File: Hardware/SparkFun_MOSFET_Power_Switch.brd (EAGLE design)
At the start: 35.6 x 34.3 mm, 56 parts, among them J3 5.5x2.1mm Barrel, Q1 600mA/40V, Q2 100A/100V/6.8mΩ, U1 LMR14203

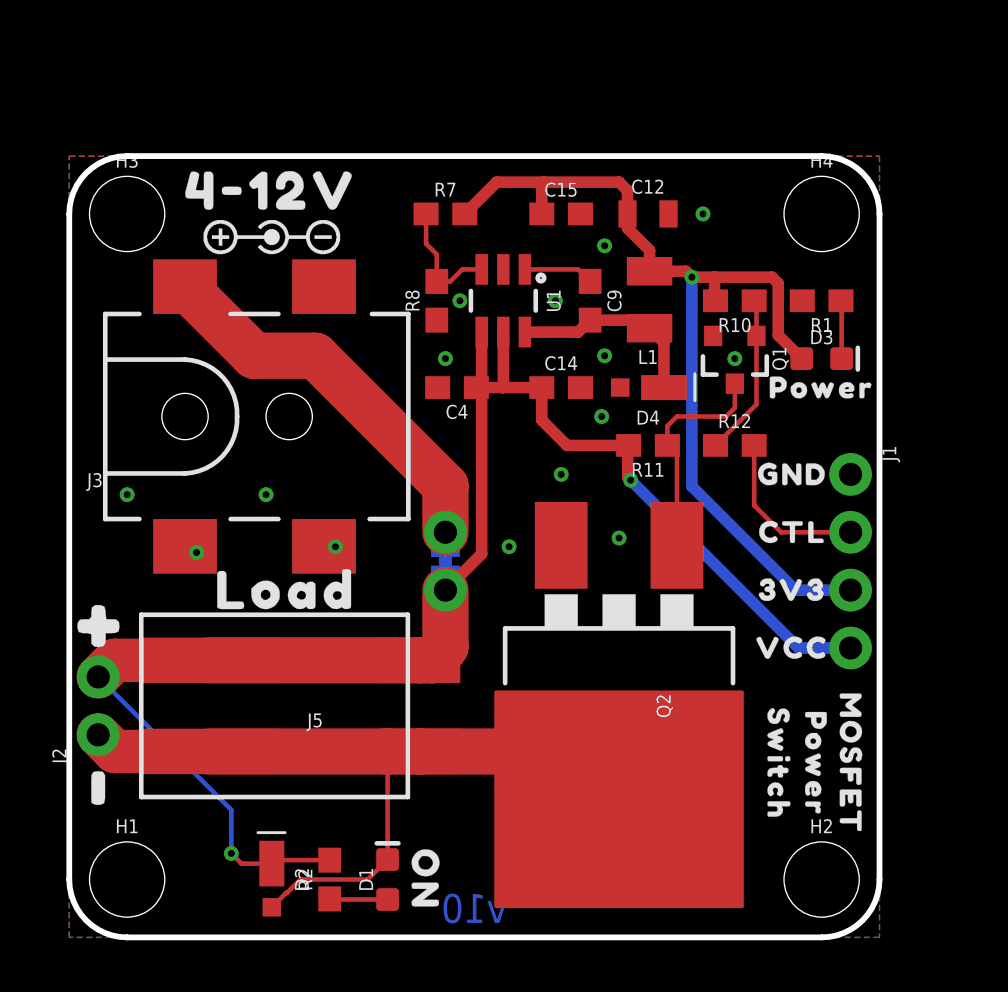
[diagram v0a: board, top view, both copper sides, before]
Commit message: add 4-pin female header
-added SMD vertical 4-pin header to allow solderless connection access to the CTRL line and more.
-Added jumpers to kill power and on LEDs
-updated silk to inverted buzzard style
-changed logo to SFE
-updated measures.
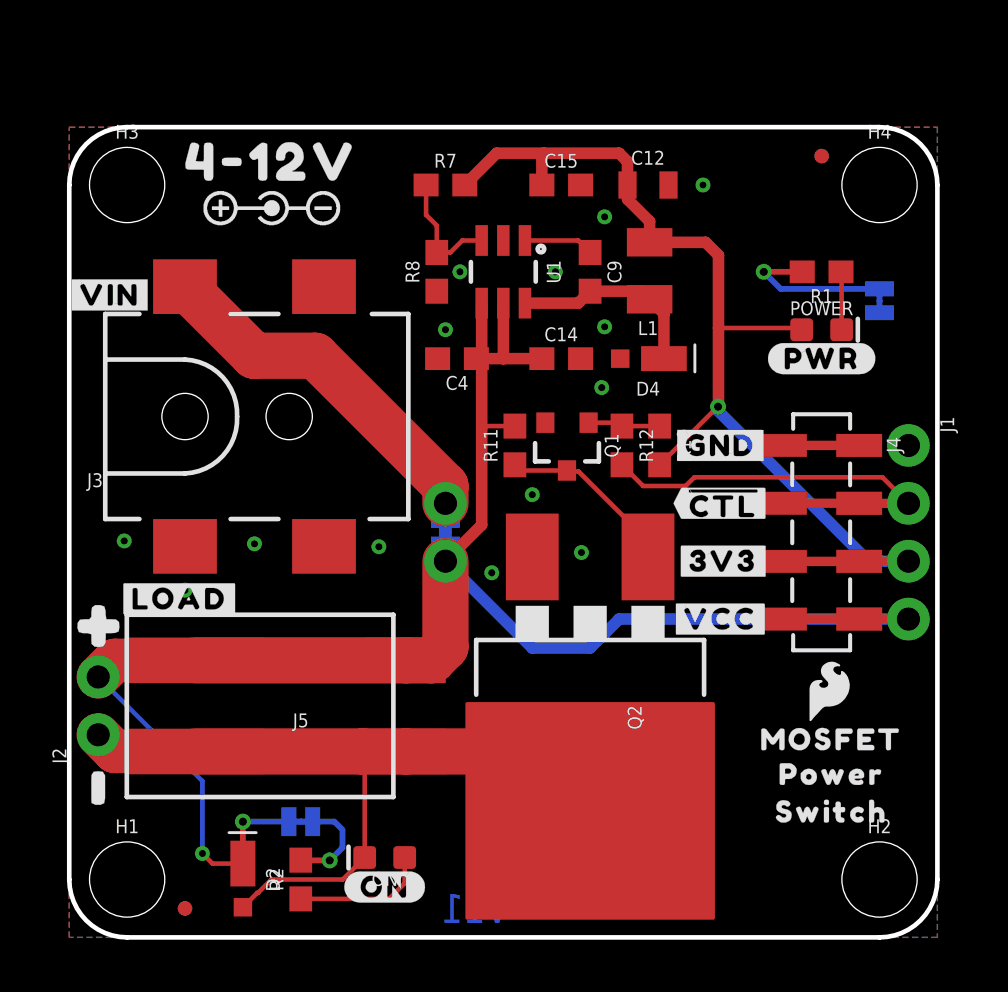
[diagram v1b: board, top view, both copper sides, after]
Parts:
- removed D1, D3: RED, SparkFun-LED:LED-0603
- removed JP2: JUMPER-COMBO_2_NC_TRACE, SparkFun-Jumpers:COMBO-JUMPER_2_NC_TRACE
- removed U$23: (no value), output:POWER0
- removed U$49: (no value), output:ON0
- added FD1, FD2, FD3, FD4: FIDUCIALUFIDUCIAL, SparkFun-Aesthetics:FIDUCIAL-MICRO
- added J4: SMD, SparkFun-Connectors:1X04_SMD_VERTICAL_COMBO
- added LOGO2: SFE_LOGO_NAME_FLAME.1_INCH, SparkFun-Aesthetics:SFE_LOGO_NAME_FLAME_.1
- added MEAS: JUMPER-COMBO_2_NC_TRACE, SparkFun-Jumpers:COMBO-JUMPER_2_NC_TRACE
- added ON, POWER: RED, SparkFun-LED:LED-0603
- added ON_LED, PWR_LED: (no value), SparkFun-Jumpers:SMT-JUMPER_2_NC_TRACE_SILK
- added U$12, U$4: (no value), output:#GND#0
- added U$14, U$27: (no value), output:#3V3#3
- added U$28: (no value), output:##CTL##1
- added U$30: (no value), output:##CTL##2
- added U$31, U$32: (no value), output:#VCC#4
- J1: value (none) -> PTH
- R7: value 3.3k -> 100k
- R8: value 1k -> 30.1k
- U$1: device output:3V32 -> output:#LOAD#7
- U$15: device output:GND0 -> output:#PWR_LED#11
- U$16: device output:CTL0 -> output:#ON_LED#13
- U$17: device output:3V32 -> output:#MEAS#14
- U$18: device output:VCC3 -> output:#VIN#8
- U$21: value SPARKX-LOGO5 -> (none); device SparkX:SPARKX-LARGE -> output:#VCC#4
- U$3: device output:GND0 -> output:#VIN#8
- U$5: device output:LOAD0 -> output:#PWR#9
- U$7: device output:VCC3 -> output:#ON#10
- U$8: device output:CTL0 -> SparkFun-Aesthetics:SFE_LOGO_FLAME_.1
- moved U$3 31.0 mm to (1.78, 28.2)
- moved U$1 26.9 mm to (4.83, 14.9)
- moved U$5 25.6 mm to (33.0, 25.4)
- moved U$16 21.0 mm to (14.8, 5.13)
- moved U$7 20.8 mm to (13.8, 2.21)
- moved U$18 18.6 mm to (14.1, 19.0)
- moved U$26 14.8 mm to (17.9, 22.5)
- moved U$25 14.6 mm to (18.0, 24.8)
- moved U$24 14.6 mm to (17.9, 27.3)
- moved U$17 13.7 mm to (18.2, 17.6), turned to 90 degrees
- moved U$21 13.3 mm to (13.9, 16.5)
- moved Q1 8.29 mm to (21.8, 21.6)
- moved U$15 7.67 mm to (30.6, 27.9)
- moved R10 7.16 mm to (25.9, 21.6), turned to 270 degrees
- moved U$8 7.14 mm to (33.4, 10.8)
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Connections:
- new net N$6: PWR_LED.2, R1.2
- new net N$7: ON_LED.1, R2.2
- net 3.3V: now also J4.3, POWER.A; no longer D3.A
- net CUTOFF: now also J4.2
- net GND: now also J4.1, PWR_LED.1; no longer R1.2
- net N$2: now also ON.A; no longer D1.A
- net N$3: now also POWER.C; no longer D3.C
- net SOLENOID: now also ON.C; no longer D1.C
- net VCC: now also J4.4, MEAS.2, MEAS.4, ON_LED.2; no longer JP2.2, JP2.4, R2.2
- net VIN: now also MEAS.1, MEAS.3; no longer JP2.1, JP2.3
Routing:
- net CUTOFF: track 7.35 -> 15.7 mm
- net VCC: track 71.0 -> 79.1 mm
- net N$6: track 0.00 -> 7.08 mm, vias 0 -> 1
- net N$7: track 0.00 -> 4.31 mm, vias 0 -> 1
- net N$12: track 7.14 -> 3.18 mm
- net N$2: track 2.55 -> 5.97 mm
- net 3.3V: track 41.9 -> 43.9 mm
- net N$1: track 9.76 -> 7.93 mm
- net VIN: track 18.0 -> 16.6 mm
- net SOLENOID: track 33.9 -> 33.1 mm
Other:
- board size 35.6 x 34.3 mm -> 38.1 x 35.6 mm
- board text added: "Nathan Seidle"
- board text added: "Revised by: Pete Lewis"
- board text added: "Units are INCHES"
- board text added: "v11"
- board text removed: "v10"

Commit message: Buck reg routing
-optimized buck reg routing
-added PTH header for VIN/GND
-added "low-side" to silk name top and bottom
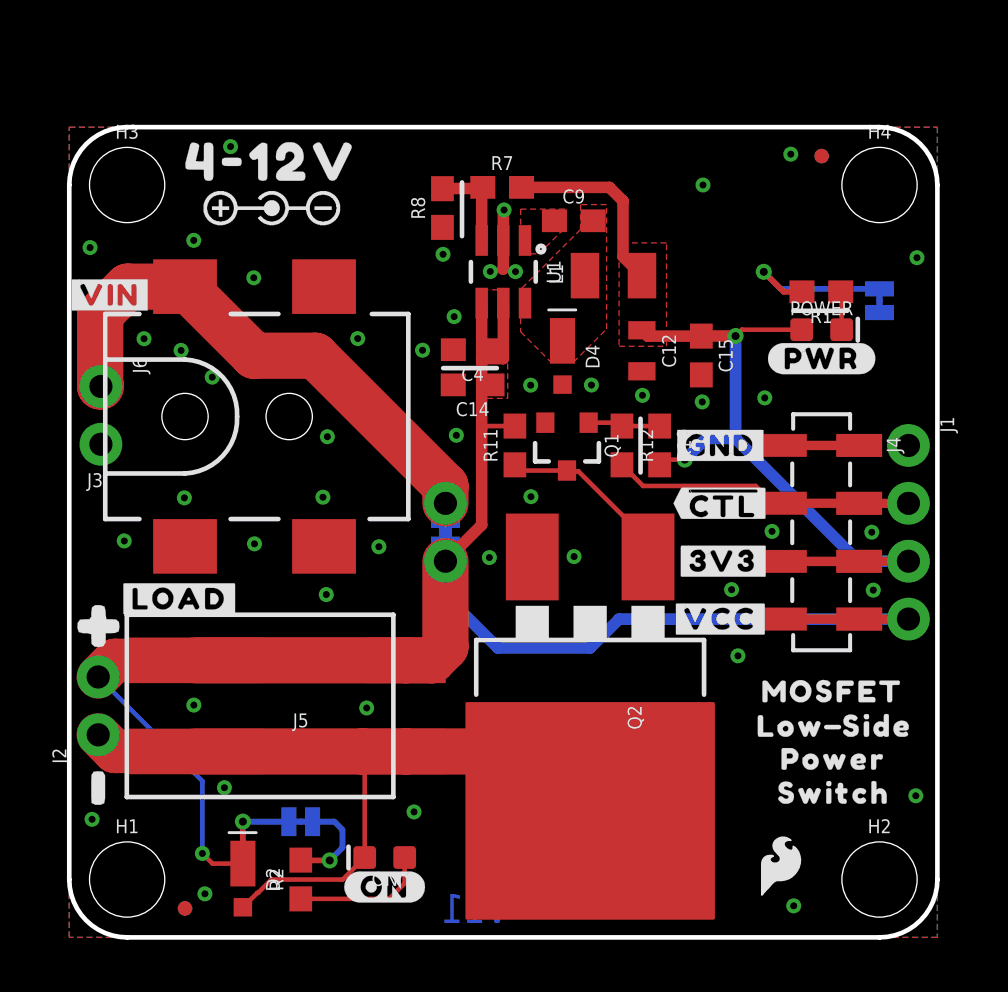
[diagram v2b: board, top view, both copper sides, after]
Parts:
- removed U$18: (no value), output:#VIN#8
- removed U$21: (no value), output:#VCC#4
- added J6: (no value), SparkFun-Connectors:1X02_NO_SILK
- added U$23: (no value), output:LOW0
- added U$33: (no value), output:SIDE0
- added U$34: (no value), output:SIDE2
- added U$35: (no value), output:LOW3
- added U$36: (no value), output:#VIN#8
- added U$37: (no value), output:#GND#0
- moved C15 9.69 mm to (27.7, 25.5), turned to 270 degrees
- moved U$8 7.96 mm to (31.2, 3.15)
- moved C12 7.28 mm to (25.1, 25.7), turned to 270 degrees
- moved C14 4.05 mm to (17.7, 24.2), turned to 180 degrees
- moved D4 3.75 mm to (21.6, 25.5), turned to 270 degrees
- moved U$17 3.27 mm to (14.9, 17.7)
- moved R8 2.81 mm to (16.4, 32.0)
- moved R7 2.49 mm to (19.0, 32.9)
- moved C9 2.35 mm to (22.1, 31.5), turned to 0 degrees
- moved U$2 2.10 mm to (33.5, 10.8)
- moved U$24 1.87 mm to (18.1, 29.1)
- moved L1 1.56 mm to (23.8, 29.1), turned to 90 degrees
- moved LOGO2 1.46 mm to (18.7, 31.4)
- moved R1 0.88 mm to (33.0, 28.3)
- moved U$13 0.83 mm to (33.6, 6.33)
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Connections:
- net CUTOFF renamed !CTL
- net SOLENOID renamed LOAD
- net GND: now also J6.2
- net VIN: now also J6.1
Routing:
- net VSW: track 8.70 -> 0.00 mm
- net 3.3V: track 43.9 -> 35.8 mm, vias 1 -> 2
- net VIN: track 16.6 -> 24.0 mm
- net N$10: track 3.08 -> 0.00 mm
- net GND: track 0.00 -> 2.63 mm, vias 15 -> 47
- net N$5: track 5.34 -> 4.08 mm
- net VCC: track 79.1 -> 78.1 mm
- net N$3: track 2.55 -> 1.68 mm
- added copper zone on layer 1, net 3.3V
- added copper zone on layer 1, net N$10
- added copper zone on layer 1, net VCC
- added copper zone on layer 1, net VSW

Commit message: updated to new KB red resistor
-updated red led and limiting resistor
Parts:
- R1: value 1k -> 4.7k
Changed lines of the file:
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@@
 <element name="ON" library="SparkFun-LED" package="LED-0603" value="RED" x="13.843" y="3.5052" smashed="yes" rot="R180">
 <attribute name="NAME" x="13.843" y="2.8702" size="0.6096" layer="25" font="vector" ratio="20" rot="R180" align="bottom-center"/>
-<attribute name="PROD_ID" value="DIO-00819" x="13.843" y="-0.3048" size="1.778" layer="27" font="vector" ratio="15" rot="R180" display="off"/>
-<attribute name="VALUE" x="13.843" y="4.1402" size="0.6096" layer="27" font="vector" ratio="20" rot="R180" align="top-center"/>
+<attribute name="PROD_ID" value="DIO-17976" x="13.843" y="-0.3048" size="1.778" layer="27" font="vector" ratio="15" rot="R180" display="off"/>
 </element>
 <element name="R2" library="SparkFun-Resistors" package="0603" value="4.7k" x="10.16" y="2.54" smashed="yes" rot="R90">
@@
 <element name="POWER" library="SparkFun-LED" package="LED-0603" value="RED" x="33.02" y="26.67" smashed="yes">
 <attribute name="NAME" x="33.02" y="27.305" size="0.6096" layer="25" font="vector" ratio="20" align="bottom-center"/>
-<attribute name="PROD_ID" value="DIO-00819" x="33.02" y="26.67" size="1.778" layer="27" font="vector" ratio="15" display="off"/>
-<attribute name="VALUE" x="33.02" y="26.035" size="0.6096" layer="27" font="vector" ratio="20" align="top-center"/>
+<attribute name="PROD_ID" value="DIO-17976" x="33.02" y="26.67" size="1.778" layer="27" font="vector" ratio="15" display="off"/>
 </element>
-<element name="R1" library="SparkFun-Resistors" package="0603" value="1k" x="33.0073" y="28.3337" smashed="yes" rot="R180">
+<element name="R1" library="SparkFun-Resistors" package="0603" value="4.7k" x="33.0073" y="28.3337" smashed="yes" rot="R180">
 <attribute name="NAME" x="33.0073" y="27.5717" size="0.6096" layer="25" font="vector" ratio="20" rot="R180" align="bottom-center"/>
-<attribute name="PROD_ID" value="RES-07856" x="33.0073" y="28.3337" size="1.778" layer="27" font="vector" ratio="15" rot="R180" display="off"/>
-<attribute name="VALUE" x="33.0073" y="29.0957" size="0.6096" layer="27" font="vector" ratio="20" rot="R180" align="top-center"/>
+<attribute name="PROD_ID" value="RES-07857" x="33.0073" y="28.3337" size="1.778" layer="27" font="vector" ratio="15" rot="R180" display="off"/>
+<attribute name="VALUE" value="4.7k" x="33.0073" y="29.0957" size="0.6096" layer="27" font="vector" ratio="20" rot="R180" align="top-center"/>
 </element>
 <element name="U$24" library="output" package="MOSFET_0" value="" x="18.120359375" y="29.14141875" smashed="yes" rot="MR0"/>

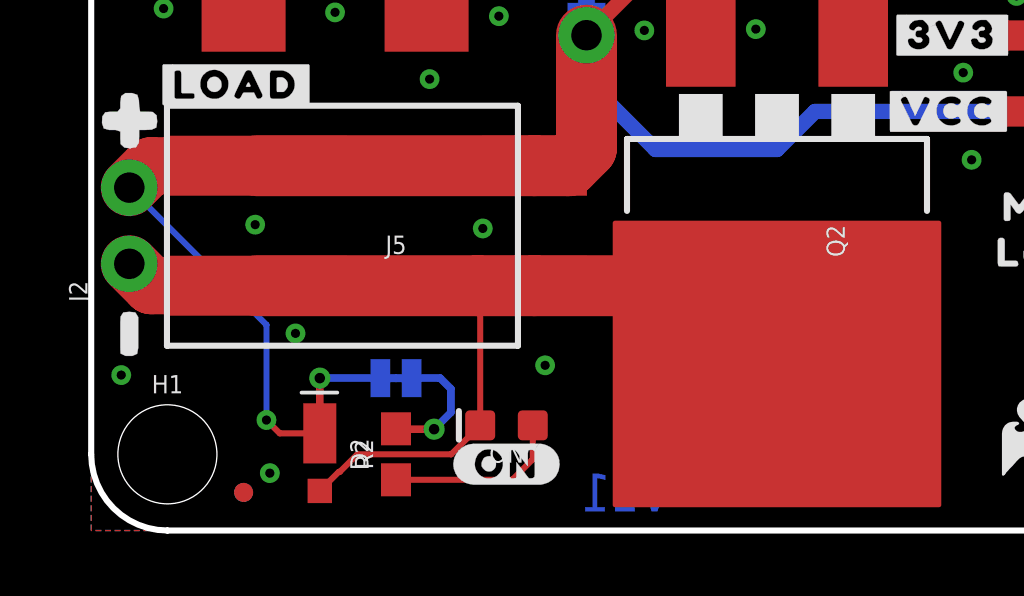
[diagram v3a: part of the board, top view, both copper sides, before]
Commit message: Re-routed Flyback Diode circuit
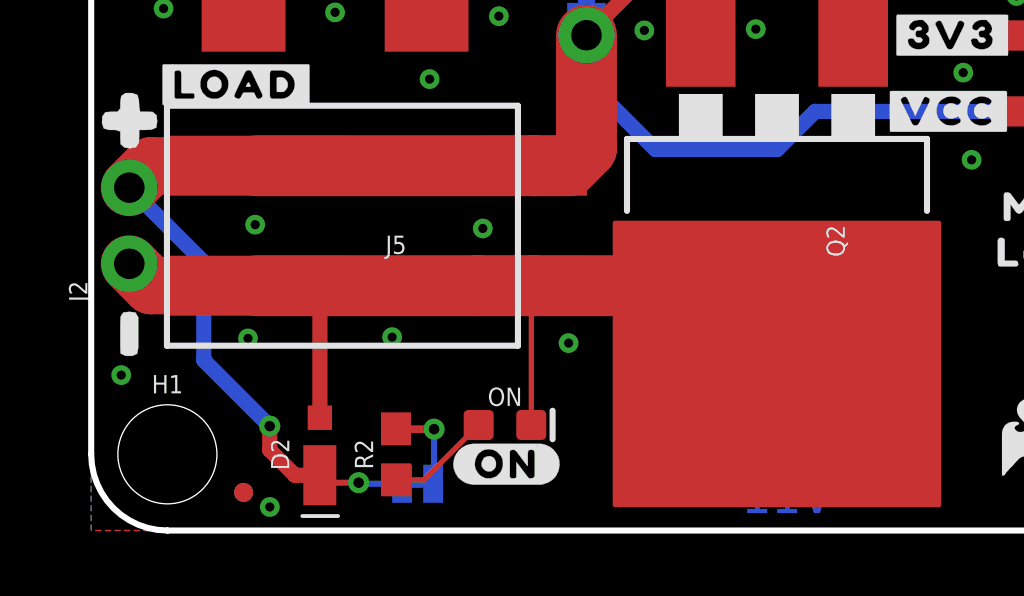
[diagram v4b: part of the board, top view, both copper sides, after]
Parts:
- moved U$16 3.62 mm to (15.5, 1.57)
- moved ON_LED 3.59 mm to (10.9, 1.56)
- moved ON 0.05 mm to (13.8, 3.52), turned to 0 degrees
- turned D2 to 90 degrees
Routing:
- net N$2: track 5.97 -> 3.51 mm
- net N$7: track 4.31 -> 3.11 mm
- net GND: vias 47 -> 48
